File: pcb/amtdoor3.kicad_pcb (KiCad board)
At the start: 2 copper layers, 65 x 30 mm, 71 parts, among them P1 CONN_01X04, P2 dnp-REF-182665-01, P3 CONN_01X04, P4 CONN_01X04, P5 CONN_01X02, P6 CONN_01X02, Q1 Q_NMOS_DUAL, Q10 Q_NMOS_DUAL, Q2 Q_PMOS_HP, Q3 DMMT3906_Dual_PNP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

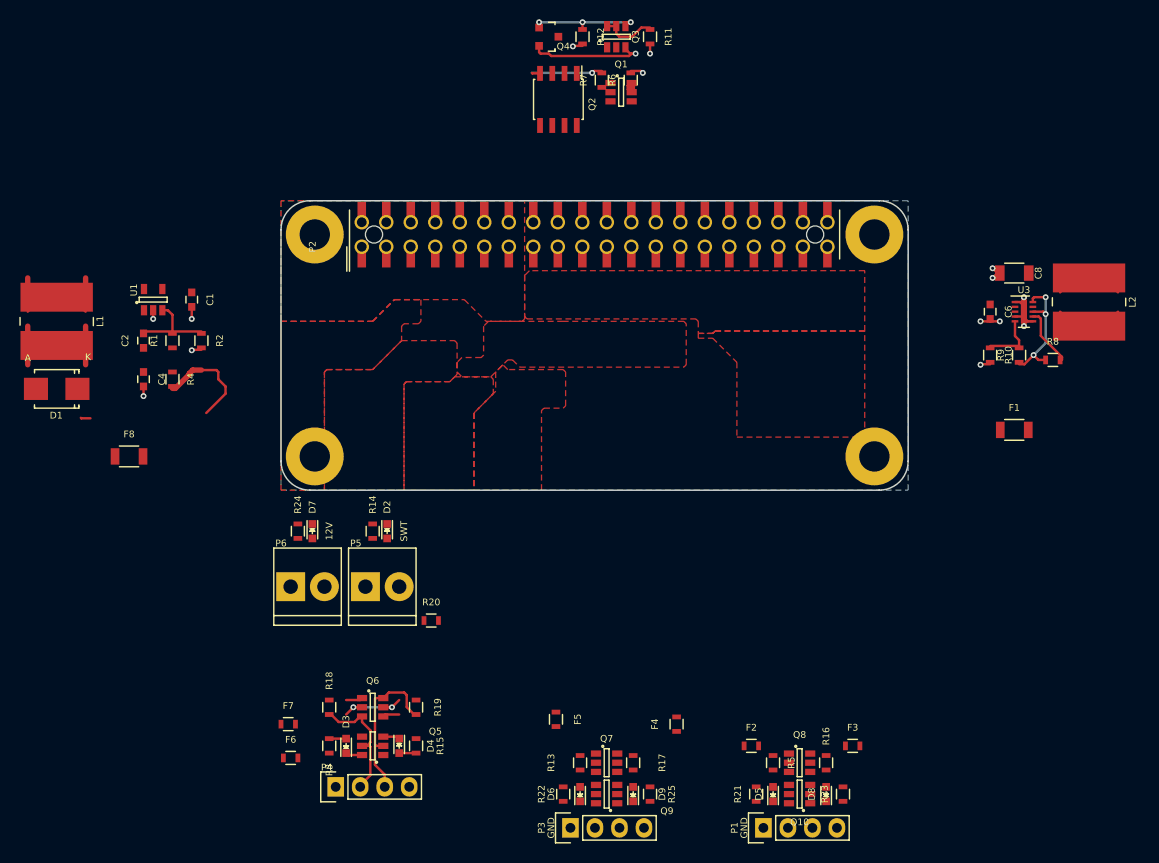
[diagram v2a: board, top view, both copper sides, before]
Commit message: new rev layout complete w/ some sch changes to help routing
* normalize boost net names
* fix boost part number to TPS62175. TPS62177 is fixed 3.3V
* DNP one option for output port voltage
* fix cap + voltage of boost/buck 12/24V decoupling caps C3, C4, C6
* reassign GPIO to ports to help routing
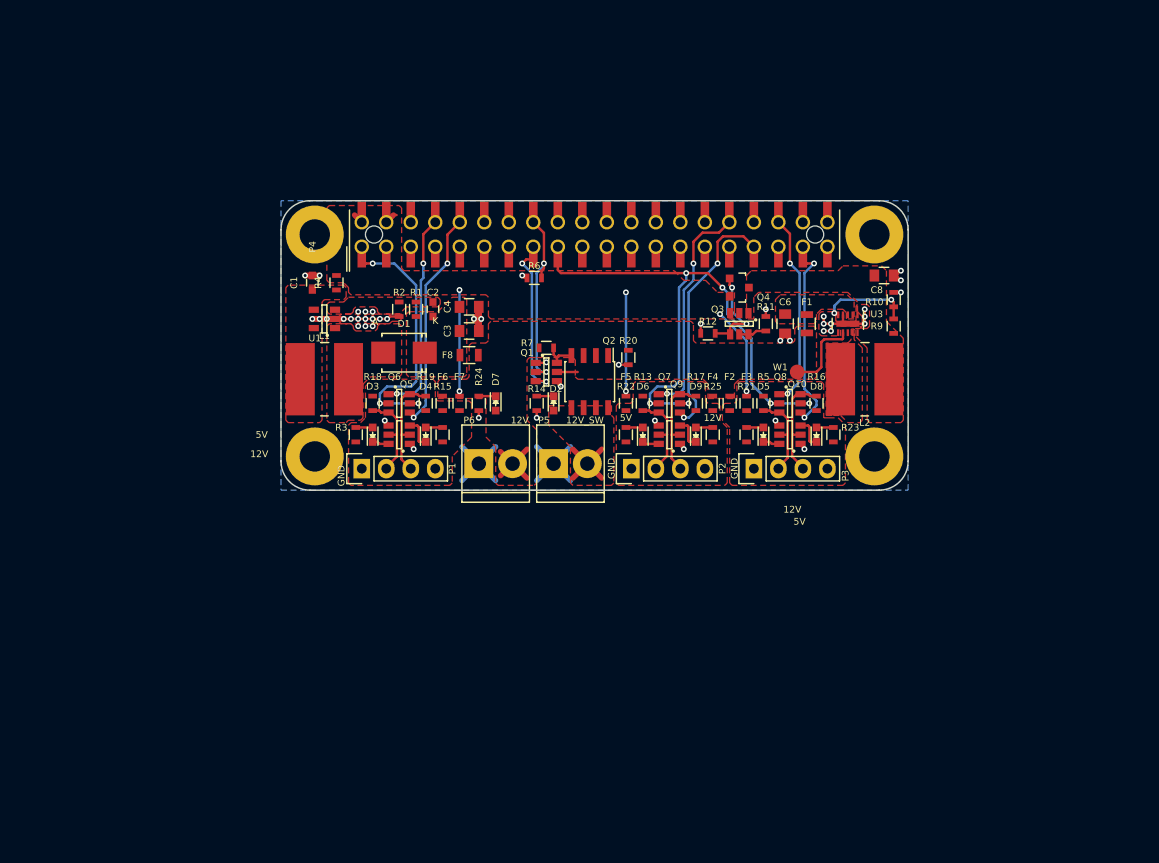
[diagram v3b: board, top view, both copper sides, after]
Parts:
- removed R8: 100k, Resistors_SMD:R_0603
- added C3: 2.2uF 50V, Capacitors_SMD:C_0805, F.Cu at (119.5, 113.5)
- added W1: TEST_1P, Measurement_Points:Measurement_Point_Round-SMD-Pad_Small, F.Cu at (153.5, 117.8)
- C4: value 4.7uF 25V -> 2.2uF 50V; footprint Capacitors_SMD:C_0603 -> Capacitors_SMD:C_0805
- C6: value 1uF -> 2.2uF 50V; footprint Capacitors_SMD:C_0603 -> Capacitors_SMD:C_0805
- C8: footprint Capacitors_SMD:C_1206 -> Capacitors_SMD:C_0805
- F1, F8: footprint Resistors_SMD:R_1206 -> Resistors_SMD:R_0805
- R10: value 383k -> 150k
- R9: value 2M -> 787k
- U3: value TPS62177 -> TPS62175
- moved F6 40.0 mm to (116.8, 121.0), turned to 90 degrees
- moved D6 37.8 mm to (137.5, 124.2)
- moved D9 37.8 mm to (143.0, 124.2)
- moved Q7 37.8 mm to (140.2, 121.0)
- moved Q9 37.8 mm to (140.2, 124.2)
- moved R13 37.8 mm to (137.5, 121.0)
- moved R17 37.8 mm to (143.0, 121.0)
- moved R22 37.8 mm to (135.8, 124.2)
- moved R25 37.8 mm to (144.8, 124.2)
- moved P2 37.8 mm to (136.3, 127.8)
- moved F7 37.7 mm to (118.5, 121.0), turned to 90 degrees
- moved D5 37.3 mm to (150.0, 124.2)
- moved D8 37.3 mm to (155.5, 124.2)
- moved Q10 37.3 mm to (152.8, 124.2)
- moved Q8 37.3 mm to (152.8, 121.0)
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- renumbered P4 to P1, P3 to P2, P1 to P3, P2 to P4
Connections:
- net /FB_5V renamed /BCK_FB
- net /SW_5V renamed /BCK_SW
- net Net-(C2-Pad1) renamed /BST_SW_D
- net Net-(C6-Pad1) renamed /P12V_BCK
- C8 pad 1: /VOS_5V -> /P5V_BCK
- L2 pad 2: /VOS_5V -> /P5V_BCK
- Q1 pad 2: /GPIO5 -> /GPIO23
- Q3 pad 1: /VOS_5V -> /P5V_BCK
- Q4 pad 3: /VOS_5V -> /P5V_BCK
- Q6 pad 2: /RPI_3V3_2 -> /RPI_3V3_1
- Q6 pad 5: /RPI_3V3_2 -> /RPI_3V3_1
- Q7 pad 1: /GPIO13 -> /GPIO12
- Q7 pad 4: /GPIO12 -> /GPIO13
- Q8 pad 1: /GPIO26 -> /GPIO16_CE2#
- Q8 pad 4: /GPIO13 -> /GPIO26
- R6 pad 1: /GPIO5 -> /GPIO23
- R9 pad 1: /VOS_5V -> /P5V_BCK
- U3 pad 10: /VOS_5V -> /P5V_BCK
- U3 pad 7: /PG_5V -> /BCK_PG
- U3 pad 8: /VOS_5V -> (no net)
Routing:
- net /RPI_3V3_2: track 7.51 -> 62.4 mm, vias 2 -> 6
- net GND: track 28.1 -> 74.9 mm, vias 14 -> 47
- net /RPI_3V3_1: track 1.31 -> 29.1 mm, vias 0 -> 3
- net /GPIO13: track 1.71 -> 27.4 mm, vias 0 -> 2
- net /VOS_5V: track 23.1 -> 0.00 mm, vias 3 -> 0
- net /GPIO12: track 1.31 -> 24.4 mm, vias 0 -> 2
- net /GPIO15_RXD0: track 3.04 -> 24.2 mm, vias 0 -> 2
- net /GPIO14_TXD0: track 1.59 -> 22.6 mm, vias 0 -> 2
- net /GPIO16_CE2#: track 1.31 -> 21.4 mm, vias 0 -> 2
- net /GPIO23: track 1.31 -> 21.0 mm, vias 0 -> 2
- net /GPIO26: track 1.31 -> 20.7 mm, vias 0 -> 2
- net +5V: track 17.4 -> 36.6 mm, vias 1 -> 6
- net /BST_SW: track 16.5 -> 0.00 mm
- net /GPIO22: track 1.31 -> 17.5 mm, vias 0 -> 2
- net /P5V_BST: track 15.5 -> 0.00 mm
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- added copper zone on F.Cu, net /BST_FB
- added copper zone on F.Cu, net /BST_SW
- added copper zone on F.Cu, net /BST_SW_D
- added copper zone on F.Cu, net /P12V_BCK
- added copper zone on F.Cu, net /P12V_SW
- added copper zone on F.Cu, net /P5V_BCK
- added copper zone on F.Cu, net /P5V_BST
- added copper zone on F.Cu, net /VPORT1
- added copper zone on F.Cu, net /VPORT2
- added copper zone on F.Cu, net /VPORT3
- added copper zone on F.Cu, net GND
- removed copper zone on F.Cu, net /SW_12V
- removed copper zone on F.Cu, net /VAUX
- removed copper zone on F.Cu, net /VOS_5V
- removed copper zone on F.Cu, net /VSWITCHED
- removed copper zone on F.Cu, net /VSWITCHED_T
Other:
- board text added: "12V_SW"
- board text added: "5V"
- board text removed: "SWT"

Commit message: pcb rev 2.0 gerbers, silk logos, routing tweaks
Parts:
- added G1: WOBBAPHAT-LOGO, amtdoor3:wobbaphat-logo-fcu, B.Cu at (101.8, 122.5)
- added G2: WOBBAPHAT-LOGO, amtdoor3:wobbaphat-logo-fsilk-lg, F.Cu at (123.0, 109.5)
- added G3: AMT-LOGO, amtdoor3:amt-logo-fcu, B.Cu at (163.2, 122.2)
- added G4: AMT-LOGO, amtdoor3:amt-logo-fsilk-lg, F.Cu at (142.5, 109.5)
- moved W1 2.46 mm to (155.8, 116.8)
- moved R10 1.77 mm to (161.8, 110.5)
- moved R9 1.77 mm to (161.8, 113.2)
- moved C8 1.03 mm to (163.5, 108.0), turned to 90 degrees
- moved U3 0.50 mm to (158.8, 112.2)
- moved L1 0.35 mm to (104.2, 118.8)
- moved L2 0.35 mm to (160.8, 118.8)
- moved C1 0.25 mm to (103.0, 108.5)
- moved R4 0.25 mm to (105.5, 108.5)
- moved U1 0.25 mm to (104.2, 112.2)
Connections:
- Q6 pad 2: /RPI_3V3_1 -> /RPI_3V3_2
- Q6 pad 5: /RPI_3V3_1 -> /RPI_3V3_2
- U3 pad 8: (no net) -> /P5V_BCK
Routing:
- net /RPI_3V3_2: track 62.4 -> 102.9 mm, vias 6 -> 9
- net /RPI_3V3_1: track 29.1 -> 1.31 mm, vias 3 -> 0
- net /GPIO26: track 20.7 -> 26.9 mm
- net +5V: track 36.6 -> 31.8 mm
- net /P5V_BCK: track 0.00 -> 3.78 mm, vias 0 -> 2
- net /BCK_PG: track 8.31 -> 5.71 mm
- net /GPIO14_TXD0: track 22.6 -> 24.9 mm
- net /GPIO16_CE2#: track 21.4 -> 23.6 mm
- net /BCK_FB: track 9.48 -> 7.47 mm
- net /GPIO15_RXD0: track 24.2 -> 25.4 mm
- net GND: track 74.9 -> 74.6 mm, vias 47 -> 46
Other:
- rule trace_min: 0.2 -> 0.2032
- rule via_min_size: 0.4 -> 0.6096
- board text added: "12-24V"
- board text added: "12/5V"
- board text added: "12|5V"
- board text added: "AMT"
- board text added: "Ian Hartwig"
- board text added: "Rev 2.0"
- board text added: "SW V"
- board text added: "WOBBApHAT"
- board text added: "WOBBApHAT Rev 2.0 Ian Hartwig - AMT"
- board text removed: "12V_SW"
